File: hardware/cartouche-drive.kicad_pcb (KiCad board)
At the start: 4 copper layers, 30 x 66 mm, 71 parts, among them J1 USB-C 105450-0101, J2 M.2 key M (2230), U1 JMS583, U2 TPS82130, U3 ZD25WQ16, Y1 25MHz 12pF

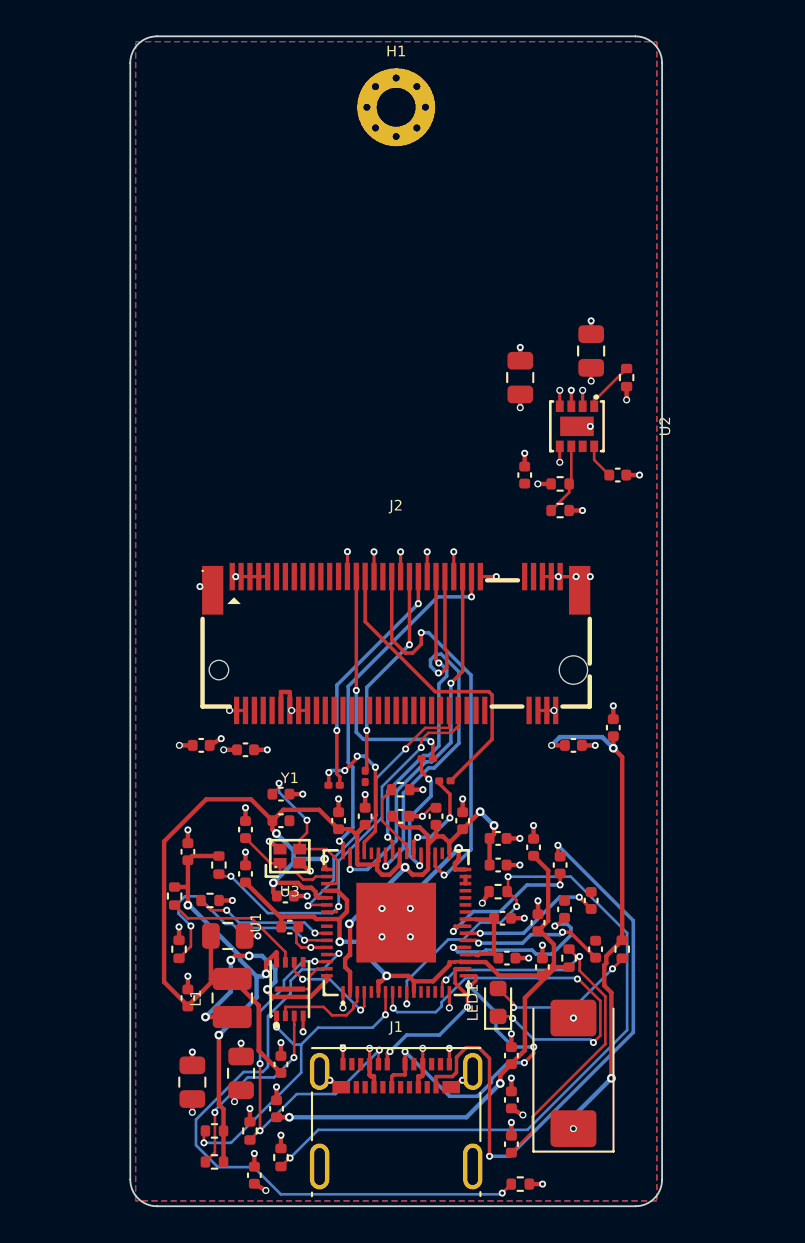
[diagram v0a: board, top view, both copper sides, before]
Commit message: PCB v0.2 WIP: fix PCIe TX/RX to M.2, new layout, scripted PCIe pairs
Schematic fix: M.2 PCIe pins are named from the host side (PET = host TX).
Our TX now goes through the 220 nF caps to PET0/PET1, RX comes from PER0/PER1.

New 36 x 46 mm layout: JMS583 under the SSD, its PCIe side facing the
socket's PCIe pins in the same order; USB-C on the left edge.
The 5 PCIe pairs are routed by the script (straight, one jog, caps staggered),
1.0 V and REXT pins on that side escape to vias inside the pin ring.
Still to do: USB 3.2 pairs (B-row vias between the two rows), power pours.
Not for fabrication yet.

Co-Authored-By: Claude Opus 5.5 <noreply@anthropic.com>
Claude-Session: https://claude.ai/code/session_01RqDGjrUG4GdEsawKGChjmB
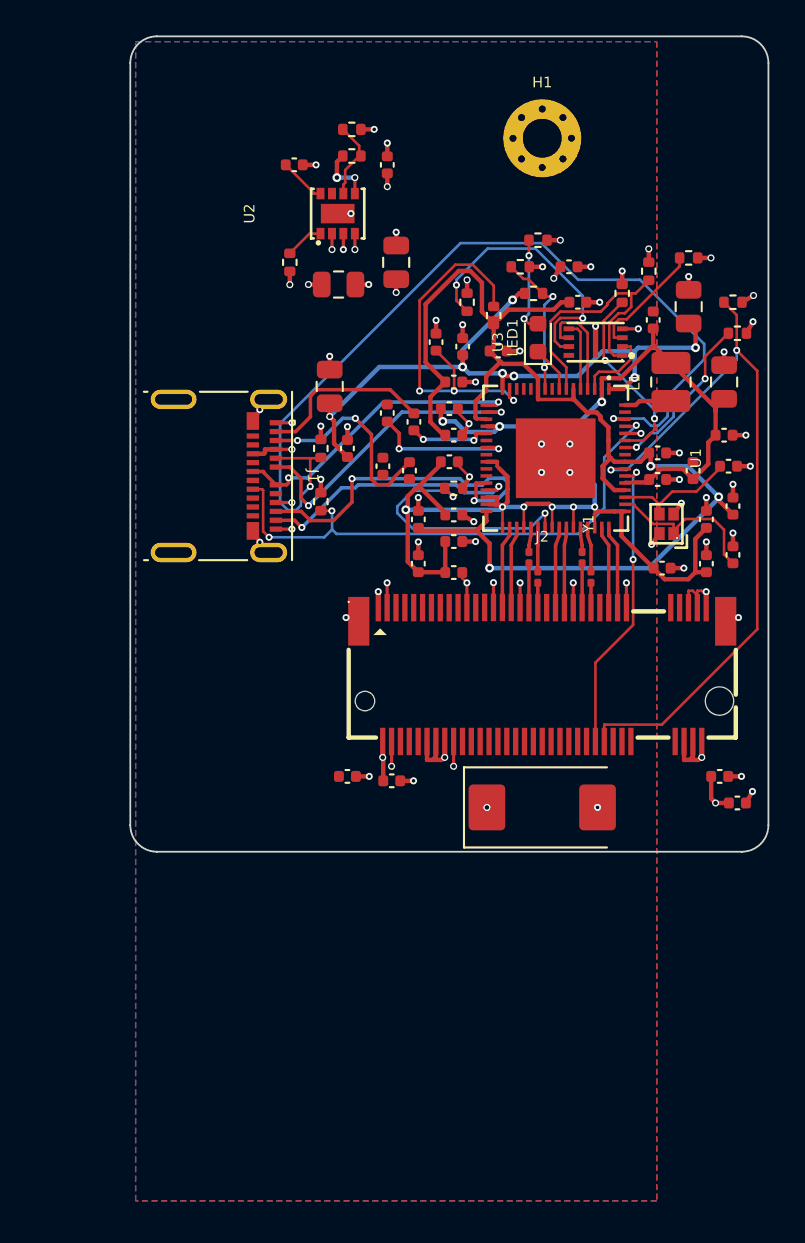
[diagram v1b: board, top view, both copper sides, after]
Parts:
- moved R11 57.6 mm to (31.5, 12.5)
- moved R10 54.3 mm to (29.2, 13.2), turned to 90 degrees
- moved R4 52.0 mm to (22.0, 13.0), turned to 0 degrees
- moved C28 50.1 mm to (31.5, 15.2)
- moved C23 48.6 mm to (25.2, 15.0), turned to 0 degrees
- moved C9 47.0 mm to (29.5, 16.0)
- moved C30 45.4 mm to (17.2, 17.2)
- moved R8 44.7 mm to (27.8, 14.5)
- moved C8 43.9 mm to (33.5, 22.5), turned to 0 degrees
- moved R7 43.7 mm to (34.2, 16.8)
- moved R13 43.0 mm to (34.0, 15.0), turned to 0 degrees
- moved L1 42.7 mm to (30.5, 19.5)
- moved C29 42.6 mm to (18.8, 17.5)
- moved C7 42.0 mm to (33.5, 19.5), turned to 90 degrees
- moved C6 41.3 mm to (12.2, 23.2)
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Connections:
- J2 pad 29: /PCIE_TXN1_M2 -> /PCIE_RXN1
- J2 pad 31: /PCIE_TXP1_M2 -> /PCIE_RXP1
- J2 pad 35: /PCIE_RXN1 -> /PCIE_TXN1_M2
- J2 pad 37: /PCIE_RXP1 -> /PCIE_TXP1_M2
- J2 pad 41: /PCIE_TXN0_M2 -> /PCIE_RXN0
- J2 pad 43: /PCIE_TXP0_M2 -> /PCIE_RXP0
- J2 pad 47: /PCIE_RXN0 -> /PCIE_TXN0_M2
- J2 pad 49: /PCIE_RXP0 -> /PCIE_TXP0_M2
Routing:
- net /VBUS_DET: track 48.1 -> 8.48 mm, vias 4 -> 2
- net /+3V3: track 63.7 -> 25.8 mm, vias 16 -> 18
- net /USB_TX2P: track 34.6 -> 0.00 mm, vias 2 -> 0
- net /VBUS: track 12.8 -> 43.8 mm
- net /CC1: track 22.1 -> 50.9 mm, vias 4 -> 2
- net /LED_K: track 22.7 -> 2.60 mm, vias 4 -> 0
- net /USB_RX2N: track 0.00 -> 19.6 mm, vias 0 -> 2
- net /PCIE_RXP1: track 23.6 -> 4.59 mm, vias 2 -> 0
- net /CLKREQ: track 23.4 -> 42.1 mm, vias 3 -> 2
- net /PCIE_RXP0: track 22.5 -> 4.53 mm, vias 2 -> 0
- net /REFCLK_N: track 20.8 -> 4.64 mm, vias 2 -> 0
- net /PCIE_TXP1_M2: track 17.2 -> 1.40 mm
- net /REFCLK_P: track 20.2 -> 4.71 mm, vias 2 -> 0
- net /USB_RX2P: track 0.00 -> 14.9 mm, vias 0 -> 2
- net /PCIE_RXN0: track 17.6 -> 4.56 mm, vias 2 -> 0
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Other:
- board size 30 x 66 mm -> 36 x 46 mm

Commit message: PCB v0.3 WIP: scripted USB 3.2 pairs, B.Cu power pours, 0201 USB caps
USB-C B row reached through vias placed between the two pad rows.
TX1/RX2 straight on F.Cu; TX2/RX1 cross on B.Cu over the In2 ground plane.
In1 and In2 are both ground; VBUS and +3V3 are pours on B.Cu, split between
the regulator's VIN and VOUT pads. USB SuperSpeed caps moved to 0201.
DRC: 0 schematic mismatch, 0 clearance on the pairs, 4 unconnected left.
Not ready for fabrication.

Co-Authored-By: Claude Opus 5.5 <noreply@anthropic.com>
Claude-Session: https://claude.ai/code/session_01RqDGjrUG4GdEsawKGChjmB
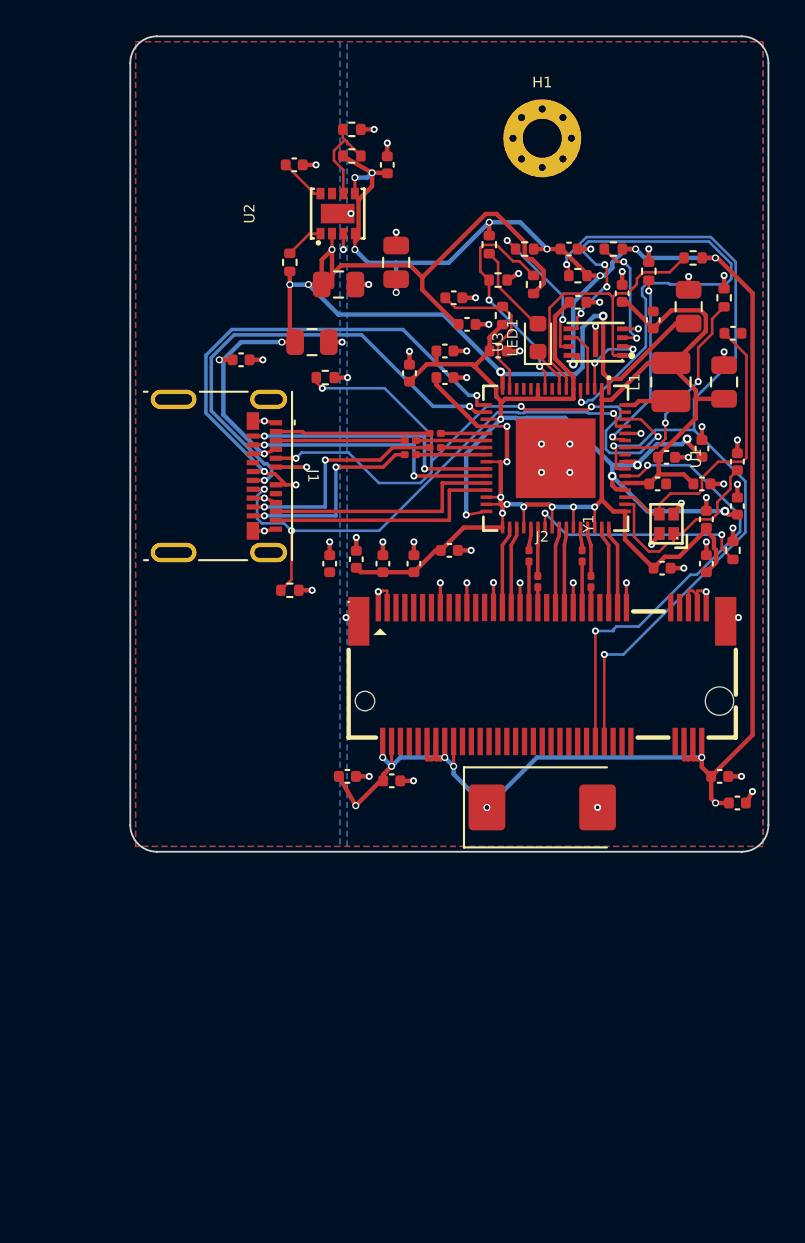
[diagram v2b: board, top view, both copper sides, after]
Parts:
- C1, C2, C3, C4: footprint Capacitor_SMD:C_0402_1005Metric -> Capacitor_SMD:C_0201_0603Metric
- moved R5 16.1 mm to (34.0, 29.0), turned to 90 degrees
- moved C15 14.2 mm to (29.8, 25.2), turned to 0 degrees
- moved C8 9.85 mm to (27.8, 14.5), turned to 90 degrees
- moved R13 8.88 mm to (25.2, 13.5)
- moved C6 7.81 mm to (6.25, 18.2), turned to 0 degrees
- moved C32 7.50 mm to (34.0, 16.8)
- moved C25 5.59 mm to (11.2, 29.8)
- moved C14 5.55 mm to (12.8, 29.5), turned to 90 degrees
- moved C17 5.49 mm to (32.5, 29.8), turned to 90 degrees
- moved R2 5.30 mm to (9.00, 31.2), turned to 0 degrees
- moved C31 5.26 mm to (34.2, 24.0)
- moved C11 5.00 mm to (18.0, 29.0)
- moved C22 4.78 mm to (17.8, 17.8)
- moved R12 4.42 mm to (22.2, 12.0), turned to 0 degrees
- moved R11 4.28 mm to (27.2, 12.0)
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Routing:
- net /+3V3: track 25.8 -> 118.9 mm
- net /VBUS: track 43.8 -> 79.3 mm, vias 12 -> 9
- net /SPI_SI: track 3.94 -> 30.9 mm, vias 0 -> 4
- net /+3V3_JMS: track 71.6 -> 55.0 mm, vias 3 -> 6
- net /USB_RX1P: track 0.00 -> 15.0 mm, vias 0 -> 2
- net /USB_RX1N: track 0.00 -> 14.9 mm, vias 0 -> 2
- net /USB_DP: track 17.3 -> 30.9 mm, vias 2 -> 3
- net /USB_TX2N: track 0.00 -> 12.9 mm, vias 0 -> 2
- net /USB_DM: track 17.1 -> 29.7 mm, vias 2 -> 3
- net /RST: track 20.8 -> 8.94 mm, vias 3 -> 0
- net /USB_TX2P: track 0.00 -> 11.6 mm, vias 0 -> 2
- net /CC1: track 50.9 -> 40.4 mm, vias 2 -> 5
- net /XOUT: track 7.03 -> 16.8 mm
- net /CLKREQ: track 42.1 -> 51.6 mm, vias 2 -> 3
- net /PERST: track 16.9 -> 25.7 mm
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- added copper zone on B.Cu, net /+3V3
- added copper zone on In2.Cu, net /GND
- added copper zone on B.Cu, net /VBUS
- removed copper zone on In2.Cu, net /+3V3
- removed copper zone on B.Cu, net /GND
- removed copper zone on In2.Cu, net /VBUS

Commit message: PCB v0.4: fab files, stitching, 1.0 V island, tighter USB pairs
- USB pairs 0.2/0.1 mm, GND stitching vias, +1V0 island on In2
- 0 unconnected, 0 parity errors in DRC
- hardware/fab: Gerbers + drill (zip), JLCPCB BOM and CPL (tools/jlc_files.py)
- LCSC: C1-C4 C76934, L1 C383386

Co-Authored-By: Claude Opus 5.5 <noreply@anthropic.com>
Claude-Session: https://claude.ai/code/session_01RqDGjrUG4GdEsawKGChjmB
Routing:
- net /+1V0: track 80.4 -> 42.8 mm, vias 9 -> 22
- net /SPI_SI: track 30.9 -> 3.94 mm, vias 4 -> 0
- net /+3V3_JMS: track 55.0 -> 78.1 mm, vias 6 -> 5
- net /CLKREQ: track 51.6 -> 31.2 mm
- net /USB_DM: track 29.7 -> 19.2 mm, vias 3 -> 2
- net /VBUS_DET: track 13.3 -> 21.9 mm
- net /PERST: track 25.7 -> 22.3 mm
- net /SPI_SCK: track 3.61 -> 6.30 mm
- net /+3V3: track 118.9 -> 116.4 mm
- net /MODE0: track 11.3 -> 13.7 mm
- net /SPI_SO: track 4.63 -> 6.82 mm, vias 2 -> 0
- net /XOUT: track 16.8 -> 15.0 mm, vias 0 -> 2
- net /USB_DP: track 30.9 -> 32.7 mm
- net /GND: track 57.4 -> 58.9 mm, vias 65 -> 216
- net /CC1: track 40.4 -> 39.0 mm, vias 5 -> 3
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- added copper zone on In2.Cu, net /+1V0
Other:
- board text added: "CARTOUCHE Drive v0.3"

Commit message: PCB v0.4 images, board label inside the outline
Co-Authored-By: Claude Opus 5.5 <noreply@anthropic.com>
Claude-Session: https://claude.ai/code/session_01RqDGjrUG4GdEsawKGChjmB
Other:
- board text added: "CARTOUCHE Drive v0.4"
- board text removed: "CARTOUCHE Drive v0.3"
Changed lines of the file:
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@@
 		(layer "Edge.Cuts")
 	)
-	(gr_text "CARTOUCHE Drive v0.3"
-		(at 4.8 43.5 0)
+	(gr_text "CARTOUCHE Drive v0.4"
+		(at 1.5 43.5 0)
 		(layer "F.SilkS")
 		(effects
 			(font
-				(size 1 1)
+				(size 0.9 0.9)
 				(thickness 0.15)
 			)
+			(justify left)
 		)
 	)
